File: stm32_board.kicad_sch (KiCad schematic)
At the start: 28 parts, among them J1 USB_B_Micro, J2 Conn_01x04_Pin, J3 Conn_01x04_Pin, J4 Conn_01x04_Pin, SW1 SW_SPDT, U1 AMS1117-3.3, U2 STM32F103C8Tx, Y1 16MHz

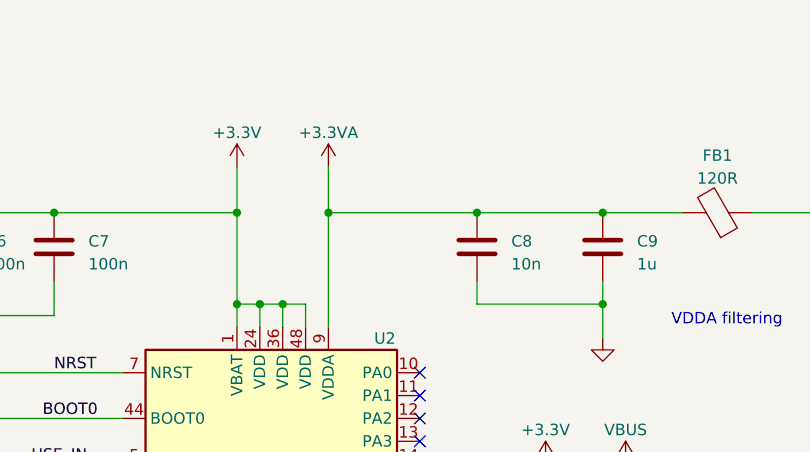
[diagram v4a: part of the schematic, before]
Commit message: Added footprints
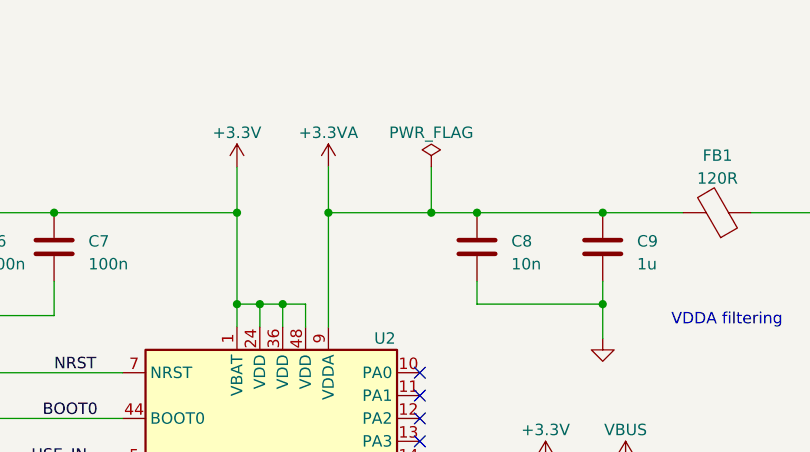
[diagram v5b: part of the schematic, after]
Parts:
- C1, C2: footprint (none) -> Capacitor_SMD:C_0805_2012Metric
- C10, C11, C12, C13, C4, C5, C6, C7, C8, C9: footprint (none) -> Capacitor_SMD:C_0402_1005Metric
- C3: footprint (none) -> Capacitor_SMD:C_0603_1608Metric
- D1: footprint (none) -> LED_SMD:LED_0603_1608Metric
- FB1: footprint (none) -> Inductor_SMD:L_0603_1608Metric
- J1: footprint (none) -> Connector_USB:USB_Micro-B_Wuerth_629105150521
- J2, J3, J4: footprint (none) -> Connector_PinHeader_2.54mm:PinHeader_1x04_P2.54mm_Vertical
- R1, R2, R3, R4, R5: footprint (none) -> Resistor_SMD:R_0402_1005Metric
- SW1: footprint (none) -> Button_Switch_THT:SW_E-Switch_EG1224_SPDT_Angled
- Y1: footprint (none) -> Crystal:Crystal_SMD_3225-4Pin_3.2x2.5mm
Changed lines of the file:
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@@
   (junction (at 106.68 55.88) (diameter 0) (color 0 0 0 0)
+  )
+  (junction (at 200.66 44.45) (diameter 0) (color 0 0 0 0)
   )
   (junction (at 158.75 44.45) (diameter 0) (color 0 0 0 0)
@@
     (stroke (width 0) (type default))
   )
+  (wire (pts (xy 200.66 39.37) (xy 200.66 44.45))
+    (stroke (width 0) (type default))
+  )
   (wire (pts (xy 41.91 41.91) (xy 41.91 48.26))
     (stroke (width 0) (type default))
@@
     (stroke (width 0) (type default))
   )
+  (wire (pts (xy 200.66 44.45) (xy 205.74 44.45))
+    (stroke (width 0) (type default))
+  )
   (wire (pts (xy 199.39 95.25) (xy 212.09 95.25))
     (stroke (width 0) (type default))
@@
     (stroke (width 0) (type default))
   )
-  (wire (pts (xy 189.23 44.45) (xy 205.74 44.45))
+  (wire (pts (xy 189.23 44.45) (xy 200.66 44.45))
     (stroke (width 0) (type default))
   )
@@
       (effects (font (size 1.27 1.27)))
     )
-    (property "Footprint" "" (at 148.59 69.088 90)
+    (property "Footprint" "Resistor_SMD:R_0402_1005Metric" (at 148.59 69.088 90)
       (effects (font (size 1.27 1.27)) hide)
     )
@@
       (effects (font (size 1.27 1.27)))
     )
-    (property "Footprint" "" (at 111.76 113.03 0)
+    (property "Footprint" "Connector_PinHeader_2.54mm:PinHeader_1x04_P2.54mm_Vertical" (at 111.76 113.03 0)
       (effects (font (size 1.27 1.27)) hide)
     )
@@
       (effects (font (size 1.27 1.27)) (justify left))
     )
-    (property "Footprint" "" (at 125.222 132.08 90)
+    (property "Footprint" "Resistor_SMD:R_0402_1005Metric" (at 125.222 132.08 90)
       (effects (font (size 1.27 1.27)) hide)
     )
@@
       (effects (font (size 1.27 1.27)) (justify left))
     )
-    (property "Footprint" "" (at 134.112 132.08 90)
+    (property "Footprint" "Resistor_SMD:R_0402_1005Metric" (at 134.112 132.08 90)
       (effects (font (size 1.27 1.27)) hide)
     )
@@
       (effects (font (size 1.27 1.27)) (justify left))
     )
-    (property "Footprint" "" (at 107.6452 52.07 0)
+    (property "Footprint" "Capacitor_SMD:C_0603_1608Metric" (at 107.6452 52.07 0)
       (effects (font (size 1.27 1.27)) hide)
     )
@@
       (effects (font (size 1.27 1.27)))
     )
-    (property "Footprint" "" (at 67.31 34.29 0)
+    (property "Footprint" "LED_SMD:LED_0603_1608Metric" (at 67.31 34.29 0)
       (effects (font (size 1.27 1.27)) hide)
     )
@@
       (effects (font (size 1.27 1.27)))
     )
-    (property "Footprint" "" (at 53.34 128.27 0)
+    (property "Footprint" "Crystal:Crystal_SMD_3225-4Pin_3.2x2.5mm" (at 53.34 128.27 0)
       (effects (font (size 1.27 1.27)) hide)
     )
@@
       (effects (font (size 1.27 1.27)) (justify left))
     )
-    (property "Footprint" "" (at 136.8552 52.07 0)
+    (property "Footprint" "Capacitor_SMD:C_0402_1005Metric" (at 136.8552 52.07 0)
       (effects (font (size 1.27 1.27)) hide)
     )
@@
       (effects (font (size 1.27 1.27)) (justify right))
     )
-    (property "Footprint" "" (at 229.87 93.98 0)
+    (property "Footprint" "Connector_USB:USB_Micro-B_Wuerth_629105150521" (at 229.87 93.98 0)
       (effects (font (size 1.27 1.27)) hide)
     )
@@
     )
   )
+  (symbol (lib_id "power:PWR_FLAG") (at 200.66 39.37 0) (unit 1)
+    (in_bom yes) (on_board yes) (dnp no) (fields_autoplaced)
+    (property "Reference" "#FLG01" (at 200.66 37.465 0)
+      (effects (font (size 1.27 1.27)) hide)
+    )
+    (property "Value" "PWR_FLAG" (at 200.66 35.56 0)
+      (effects (font (size 1.27 1.27)))
+    )
+    (property "Footprint" "" (at 200.66 39.37 0)
+      (effects (font (size 1.27 1.27)) hide)
+    )
+    (property "Datasheet" "~" (at 200.66 39.37 0)
+      (effects (font (size 1.27 1.27)) hide)
+    )
+    (pin "1")
+    (instances
+      (project "stm32_board"
+        (path "/058edb5f-f5a5-4cac-aa4e-0bf18ffaa150"
+          (reference "#FLG01") (unit 1)
+        )
+      )
+    )
+  )
   (symbol (lib_id "Connector:Conn_01x04_Pin") (at 111.76 139.7 0) (unit 1)
     (in_bom yes) (on_board yes) (dnp no)
@@
       (effects (font (size 1.27 1.27)))
     )
-    (property "Footprint" "" (at 111.76 139.7 0)
+    (property "Footprint" "Connector_PinHeader_2.54mm:PinHeader_1x04_P2.54mm_Vertical" (at 111.76 139.7 0)
       (effects (font (size 1.27 1.27)) hide)
     )
@@
       (effects (font (size 1.27 1.27)) (justify left))
     )
-    (property "Footprint" "" (at 206.7052 52.07 0)
+    (property "Footprint" "Capacitor_SMD:C_0402_1005Metric" (at 206.7052 52.07 0)
       (effects (font (size 1.27 1.27)) hide)
     )
@@
       (effects (font (size 1.27 1.27)) hide)
     )
-    (property "Footprint" "" (at 135.89 88.9 0)
+    (property "Footprint" "Button_Switch_THT:SW_E-Switch_EG1224_SPDT_Angled" (at 135.89 88.9 0)
       (effects (font (size 1.27 1.27)) hide)
     )
@@
       (effects (font (size 1.27 1.27)) (justify left))
     )
-    (property "Footprint" "" (at 39.0652 142.24 0)
+    (property "Footprint" "Capacitor_SMD:C_0402_1005Metric" (at 39.0652 142.24 0)
       (effects (font (size 1.27 1.27)) hide)
     )
@@
       (effects (font (size 1.27 1.27)) (justify left))
     )
-    (property "Footprint" "" (at 247.3452 52.07 0)
+    (property "Footprint" "Capacitor_SMD:C_0402_1005Metric" (at 247.3452 52.07 0)
       (effects (font (size 1.27 1.27)) hide)
     )
@@
       (effects (font (size 1.27 1.27)) (justify left))
     )
-    (property "Footprint" "" (at 159.7152 52.07 0)
+    (property "Footprint" "Capacitor_SMD:C_0402_1005Metric" (at 159.7152 52.07 0)
       (effects (font (size 1.27 1.27)) hide)
     )
@@
       (effects (font (size 1.27 1.27)))
     )
-    (property "Footprint" "" (at 232.41 46.228 90)
+    (property "Footprint" "Inductor_SMD:L_0603_1608Metric" (at 232.41 46.228 90)
       (effects (font (size 1.27 1.27)) hide)
     )
@@
       (effects (font (size 1.27 1.27)) (justify left))
     )
-    (property "Footprint" "" (at 26.3652 44.45 0)
+    (property "Footprint" "Capacitor_SMD:C_0805_2012Metric" (at 26.3652 44.45 0)
       (effects (font (size 1.27 1.27)) hide)
     )
@@
       (effects (font (size 1.27 1.27)) (justify left))
     )
-    (property "Footprint" "" (at 220.6752 52.07 0)
+    (property "Footprint" "Capacitor_SMD:C_0402_1005Metric" (at 220.6752 52.07 0)
       (effects (font (size 1.27 1.27)) hide)
     )
@@
       (effects (font (size 1.27 1.27)) (justify left))
     )
-    (property "Footprint" "" (at 126.6952 69.85 0)
+    (property "Footprint" "Capacitor_SMD:C_0402_1005Metric" (at 126.6952 69.85 0)
       (effects (font (size 1.27 1.27)) hide)
     )
@@
       (effects (font (size 1.27 1.27)) (justify left))
     )
-    (property "Footprint" "" (at 148.2852 52.07 0)
+    (property "Footprint" "Capacitor_SMD:C_0402_1005Metric" (at 148.2852 52.07 0)
       (effects (font (size 1.27 1.27)) hide)
     )
@@
       (effects (font (size 1.27 1.27)) (justify left))
     )
-    (property "Footprint" "" (at 74.422 40.64 90)
+    (property "Footprint" "Resistor_SMD:R_0402_1005Metric" (at 74.422 40.64 90)
       (effects (font (size 1.27 1.27)) hide)
     )
@@
       (effects (font (size 1.27 1.27)))
     )
-    (property "Footprint" "" (at 233.68 116.84 0)
+    (property "Footprint" "Connector_PinHeader_2.54mm:PinHeader_1x04_P2.54mm_Vertical" (at 233.68 116.84 0)
       (effects (font (size 1.27 1.27)) hide)
     )
@@
       (effects (font (size 1.27 1.27)) (justify left))
     )
-    (property "Footprint" "" (at 58.1152 44.45 0)
+    (property "Footprint" "Capacitor_SMD:C_0805_2012Metric" (at 58.1152 44.45 0)
       (effects (font (size 1.27 1.27)) hide)
     )
@@
       (effects (font (size 1.27 1.27)) (justify left))
     )
-    (property "Footprint" "" (at 67.0052 142.24 0)
+    (property "Footprint" "Capacitor_SMD:C_0402_1005Metric" (at 67.0052 142.24 0)
       (effects (font (size 1.27 1.27)) hide)
     )
@@
       (effects (font (size 1.27 1.27)) (justify left))
     )
-    (property "Footprint" "" (at 124.1552 52.07 0)
+    (property "Footprint" "Capacitor_SMD:C_0402_1005Metric" (at 124.1552 52.07 0)
       (effects (font (size 1.27 1.27)) hide)
     )
@@
       (effects (font (size 1.27 1.27)) (justify left))
     )
-    (property "Footprint" "" (at 211.582 80.01 90)
-      (effects (font (size 1.27 1.27)) hide)
-    )
+    (property "Footprint" "Resistor_SMD:R_0402_1005Metric" (at 211.582 80.01 90)
+      (effects (font (size 1.27 1.27)) hide)
+    )

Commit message: Added image, updated README
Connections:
- net USART_RX renamed USART1_RX
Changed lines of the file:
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@@
     (effects (font (size 1.27 1.27)) (justify left bottom))
   )
-  (label "USART_RX" (at 154.94 107.95 0) (fields_autoplaced)
+  (label "USART1_RX" (at 154.94 107.95 0) (fields_autoplaced)
     (effects (font (size 1.27 1.27)) (justify left bottom))
   )

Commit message: Updated PCB and added step file
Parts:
- SW1: footprint Button_Switch_THT:SW_E-Switch_EG1224_SPDT_Angled -> Button_Switch_SMD:SW_SPDT_PCM12
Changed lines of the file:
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@@
       (effects (font (size 1.27 1.27)) hide)
     )
-    (property "Footprint" "Button_Switch_THT:SW_E-Switch_EG1224_SPDT_Angled" (at 135.89 88.9 0)
+    (property "Footprint" "Button_Switch_SMD:SW_SPDT_PCM12" (at 135.89 88.9 0)
       (effects (font (size 1.27 1.27)) hide)
     )

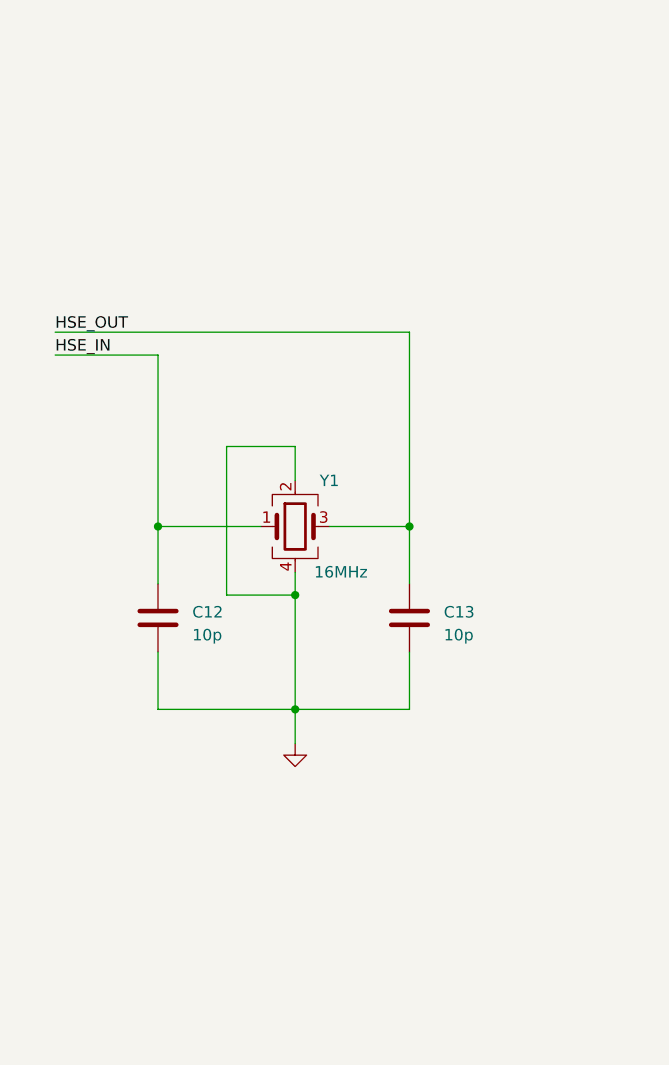
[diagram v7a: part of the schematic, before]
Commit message: Finished PCB routing
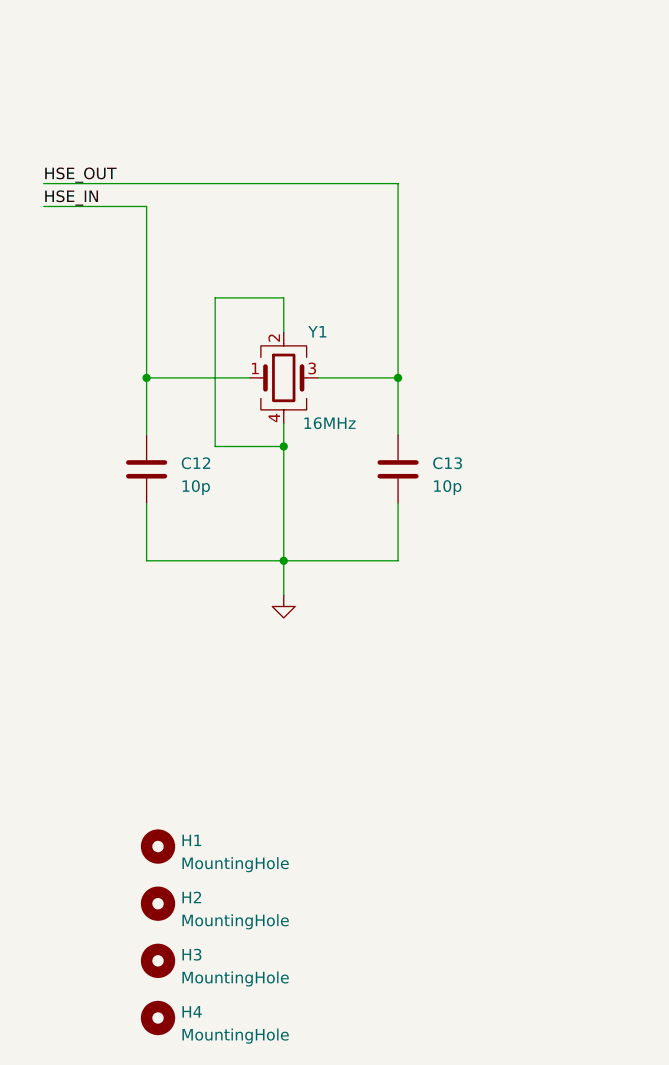
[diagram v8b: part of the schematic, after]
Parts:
- added H1, H2, H3, H4: MountingHole, MountingHole:MountingHole_2.2mm_M2, symbol Mechanical:MountingHole
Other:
- moved on the sheet: C12, C13, Y1
